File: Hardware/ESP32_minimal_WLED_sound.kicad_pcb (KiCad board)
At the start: 2 copper layers, 33.8 x 43.9 mm, 39 parts, among them J1 Conn_01x04_Male, J3 Conn_01x02_Male, Q1 AO3400A, U1 LM1117-3.3, U2 ESP32-S2-WROVER, U3 USBLC6-2SC6, U4 TXS0102DCT

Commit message: update to V1
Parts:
- removed D1: LED, LED_SMD:LED_0603_1608Metric
- removed FB1, FB2: >1A, Inductor_SMD:L_0603_1608Metric
- removed JP2: SolderJumper_3_Bridged12, Jumper:SolderJumper-3_P1.3mm_Bridged12_Pad1.0x1.5mm
- added G***: LOGO, LOGO, B.Cu at (123.6, 68.5)
- added J2: USB_C_Receptacle_USB2.0, Connector_USB:USB_C_Receptacle_HRO_TYPE-C-31-M-12, F.Cu at (145.0, 67.0)
- added J4: Barrel_Jack_Switch_Pin3Ring, Connector_BarrelJack:BarrelJack_GCT_DCJ200-10-A_Horizontal, F.Cu at (142.1, 85.2)
- added J5: Conn_01x03_Male, Connector_JST:JST_EH_B3B-EH-A_1x03_P2.50mm_Vertical, F.Cu at (119.4, 88.9)
- added J6: Conn_01x03_Male, Connector_JST:JST_EH_B3B-EH-A_1x03_P2.50mm_Vertical, F.Cu at (119.4, 93.5)
- added J7: Conn_01x03_Male, Connector_PinHeader_2.54mm:PinHeader_1x03_P2.54mm_Vertical, F.Cu at (119.4, 88.9)
- added J8: Conn_01x02_Male, TerminalBlock_Phoenix:TerminalBlock_Phoenix_MKDS-1,5-2-5.08_1x02_P5.08mm_Horizontal, F.Cu at (137.6, 91.0)
- added J9: Conn_01x03_Male, Connector_PinHeader_2.54mm:PinHeader_1x03_P2.54mm_Vertical, F.Cu at (119.4, 93.5)
- added MK1: ICS-43434, ICS-43434:MIC_ICS-43434, F.Cu at (118.7, 84.1)
- added R14: 4,7k, Resistor_SMD:R_0603_1608Metric, F.Cu at (125.2, 94.4)
- added R15: 4,7k, Resistor_SMD:R_0603_1608Metric, F.Cu at (128.3, 94.4)
- added SW2: Boot, Button_Switch_SMD:SW_SPST_B3U-1000P-B, F.Cu at (128.4, 83.8)
- added U5: ESP32-WROOM-32, RF_Module:ESP32-WROOM-32, F.Cu at (124.3, 71.6)
- C1, C2: moved to B.Cu
- C10, C11: footprint Capacitor_SMD:C_0603_1608Metric_Pad1.08x0.95mm_HandSolder -> Capacitor_SMD:C_0603_1608Metric
- C3, C4: value 20p -> 0.1uF; footprint Capacitor_SMD:C_0603_1608Metric -> Capacitor_SMD:C_0805_2012Metric; moved to B.Cu
- C5: value 0.1u -> 0.1uF
- C9: value 0.1u -> 0.1uF; footprint Capacitor_SMD:C_0603_1608Metric -> Capacitor_SMD:C_0805_2012Metric
- J1: footprint Connector_PinHeader_2.54mm:PinHeader_1x04_P2.54mm_Horizontal -> Connector_PinHeader_2.54mm:PinHeader_1x04_P2.54mm_Vertical
- J3: footprint Connector_Phoenix_MSTB:PhoenixContact_MSTBA_2,5_2-G-5,08_1x02_P5.08mm_Horizontal -> TerminalBlock_Phoenix:TerminalBlock_Phoenix_MKDS-1,5-2-5.08_1x02_P5.08mm_Horizontal
- JP1: value SolderJumper_2_Bridged -> SolderJumper_3_Open; footprint Jumper:SolderJumper-2_P1.3mm_Bridged_RoundedPad1.0x1.5mm -> Jumper:SolderJumper-3_P1.3mm_Open_Pad1.0x1.5mm; moved to B.Cu
- R1: value 10k -> 1M
- R12, R13: footprint Capacitor_SMD:C_0603_1608Metric_Pad1.08x0.95mm_HandSolder -> Resistor_SMD:R_0603_1608Metric
- R2: value 100r -> 0.01; footprint Resistor_SMD:R_0603_1608Metric -> Resistor_SMD:R_0805_2012Metric
- R3, R4: value 22r -> 10
- R6, R7, R9: footprint Resistor_SMD:R_0805_2012Metric -> Resistor_SMD:R_0603_1608Metric
- R8: value 100r -> 100
- U1: value LM1117-3.3 -> LM1117-5; moved to B.Cu
- U2: value ESP32-S2-WROVER -> INA226; footprint RF_Module:ESP32-S2-WROVER -> Package_SO:VSSOP-10_3x3mm_P0.5mm
- U3: value USBLC6-2SC6 -> LM1117-3.3; footprint Package_TO_SOT_SMD:SOT-23-6 -> Package_TO_SOT_SMD:SOT-223; moved to B.Cu
- moved R12 72.5 mm to (113.8, 83.8), turned to -90 degrees
- moved C6 68.4 mm to (131.7, 83.8), turned to -90 degrees
- moved R13 67.0 mm to (112.1, 83.8), turned to -90 degrees
- moved R4 66.9 mm to (129.6, 89.5)
- moved C7 62.1 mm to (113.8, 64.4), turned to -90 degrees
- moved R3 59.5 mm to (129.6, 91.3), turned to 180 degrees
- moved R5 58.0 mm to (112.3, 64.4), turned to -90 degrees
- moved JP1 56.6 mm to (140.1, 80.5), turned to 90 degrees
- moved C9 51.1 mm to (125.0, 85.2), turned to 90 degrees
- moved C1 50.7 mm to (137.2, 85.7), turned to 90 degrees
- moved D2 47.9 mm to (135.6, 74.8), turned to 180 degrees
- moved R2 42.8 mm to (133.6, 90.3), turned to -90 degrees
- moved J3 41.7 mm to (143.7, 80.3), turned to 90 degrees
- moved C10 39.7 mm to (113.0, 81.5)
- moved R1 39.6 mm to (141.4, 61.0), turned to 180 degrees
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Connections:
- C1 pad 1: +5V -> +12VA
- C2 pad 2: +3V3 -> +5V
- C3 pad 1: GND -> +5V
- C3 pad 2: /USB_D+ -> GND
- C4 pad 1: /USB_D- -> GND
- C4 pad 2: GND -> +3V3
- C5 pad 1: /EN -> +12VA
- C5 pad 2: GND -> +12V
- C6 pad 1: /IO00 -> IO00
- C7 pad 2: GND -> EN
- C8 pad 2: Net-(C8-Pad2) -> /U_GND
- C9 pad 1: VBUS -> +3V3
- J1 pad 2: +5VD -> Net-(J1-Pad2)
- J1 pad 3: +3V3 -> Net-(J1-Pad3)
- J1 pad 4: +12V -> +3V3
- JP1 pad 1: +3V3 -> +5V
- JP1 pad 2: Net-(JP1-Pad2) -> /O1V
- R1 pad 1: +3V3 -> /U_GND
- R1 pad 2: unconnected-(R1-Pad2) -> GND
- R12 pad 2: WS2812B_GPIO_0 -> WS2812B_2
- R13 pad 2: WS2812B_GPIO_0 -> WS2812B_4
- R2 pad 1: Net-(D1-Pad2) -> +12VA
- R2 pad 2: unconnected-(R2-Pad2) -> +12V
- R3 pad 1: /USB_D+ -> +12V
- R3 pad 2: unconnected-(R3-Pad2) -> Net-(R3-Pad2)
- R4 pad 1: /USB_D- -> Net-(R4-Pad1)
- R4 pad 2: unconnected-(R4-Pad2) -> +12VA
- R5 pad 2: /EN -> EN
- R8 pad 1: Net-(JP1-Pad2) -> +3V3
- U1 pad 2: +3V3 -> +5V
- U1 pad 3: +5V -> +12VA
- U2 pad 10: unconnected-(U2-Pad10) -> Net-(R3-Pad2)
- U2 pad 2: unconnected-(U2-Pad2) -> GND
- U2 pad 3: /IO00 -> unconnected-(U2-Pad3)
- U2 pad 4: unconnected-(U2-Pad4) -> SD
- U2 pad 5: unconnected-(U2-Pad5) -> SCK
- U2 pad 6: unconnected-(U2-Pad6) -> +3V3
- U2 pad 7: unconnected-(U2-Pad7) -> GND
- U2 pad 9: unconnected-(U2-Pad9) -> Net-(R4-Pad1)
- U3 pad 1: /D- -> GND
- U3 pad 2: GND -> +3V3
- U3 pad 3: /D+ -> +5V
- U3 pad 4: /USB_D+ -> (no net)
- U4 pad 4: GPIO_0 -> GPIO_4
- U4 pad 5: GPIO_0 -> GPIO_2
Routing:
- net +3V3: track 0.00 -> 96.4 mm, vias 0 -> 2
- net +5V: track 0.00 -> 95.5 mm, vias 0 -> 3
- net SD: track 0.00 -> 48.6 mm, vias 0 -> 3
- net +12VA: track 0.00 -> 37.9 mm, vias 0 -> 3
- net SCK: track 0.00 -> 23.7 mm, vias 0 -> 2
- net GPIO_4: track 0.00 -> 21.5 mm, vias 0 -> 2
- net GPIO_2: track 0.00 -> 19.9 mm, vias 0 -> 2
- net +12V: track 0.00 -> 15.4 mm
- net GND: track 0.00 -> 15.0 mm, vias 0 -> 21
- net WS: track 0.00 -> 14.7 mm
- net /O1: track 0.00 -> 13.0 mm
- net /O1V: track 0.00 -> 11.2 mm
- net WS2812B_4: track 0.00 -> 10.8 mm
- net Net-(R12-Pad1): track 0.00 -> 7.82 mm, vias 0 -> 2
- net Net-(Q1-Pad2): track 0.00 -> 7.21 mm
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- added copper zone on F.Cu, net /U_GND
- added copper zone on B.Cu, net GND
- added copper zone on F.Cu, net GND
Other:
- board size 33.8 x 43.9 mm -> 37.4 x 39.8 mm
- board text added: "ESP32_minimal_WLED_sound V1"

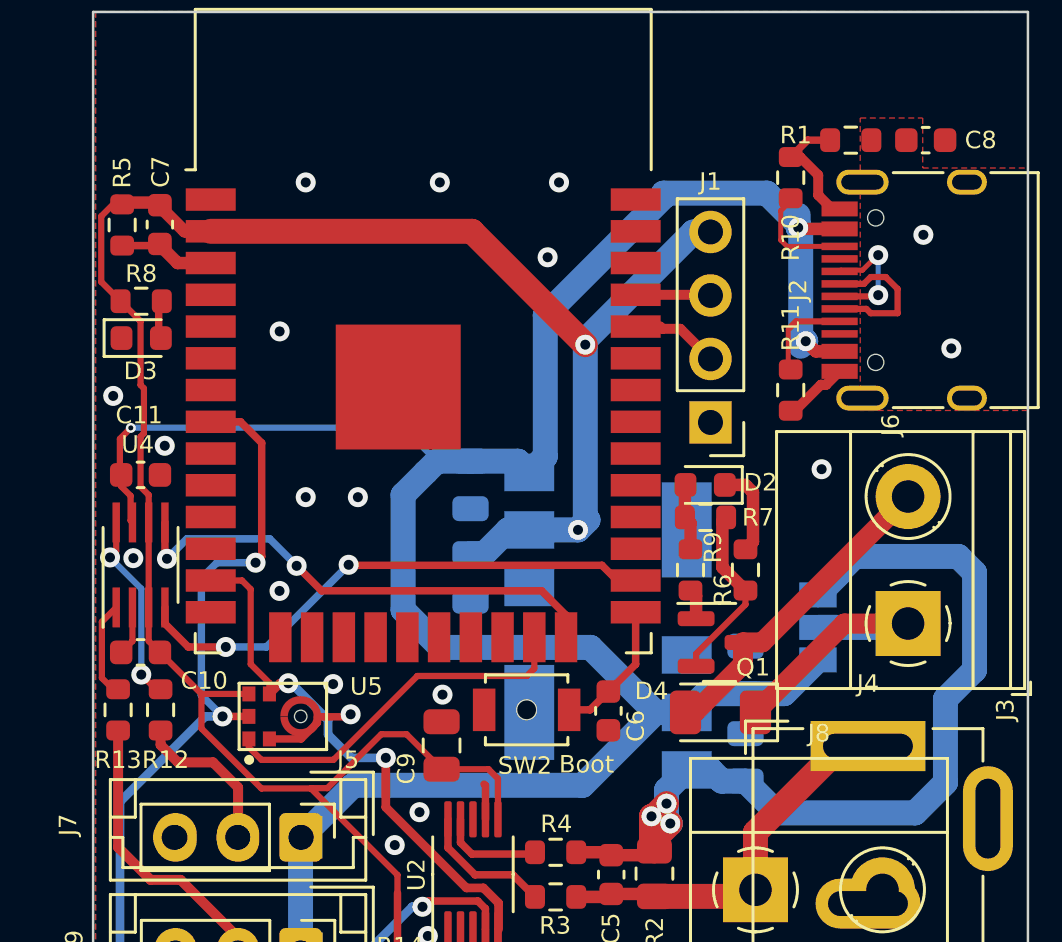
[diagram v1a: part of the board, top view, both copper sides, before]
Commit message: fix esp32 EN and IO0, Todo: solder jumper and 12V to 5V
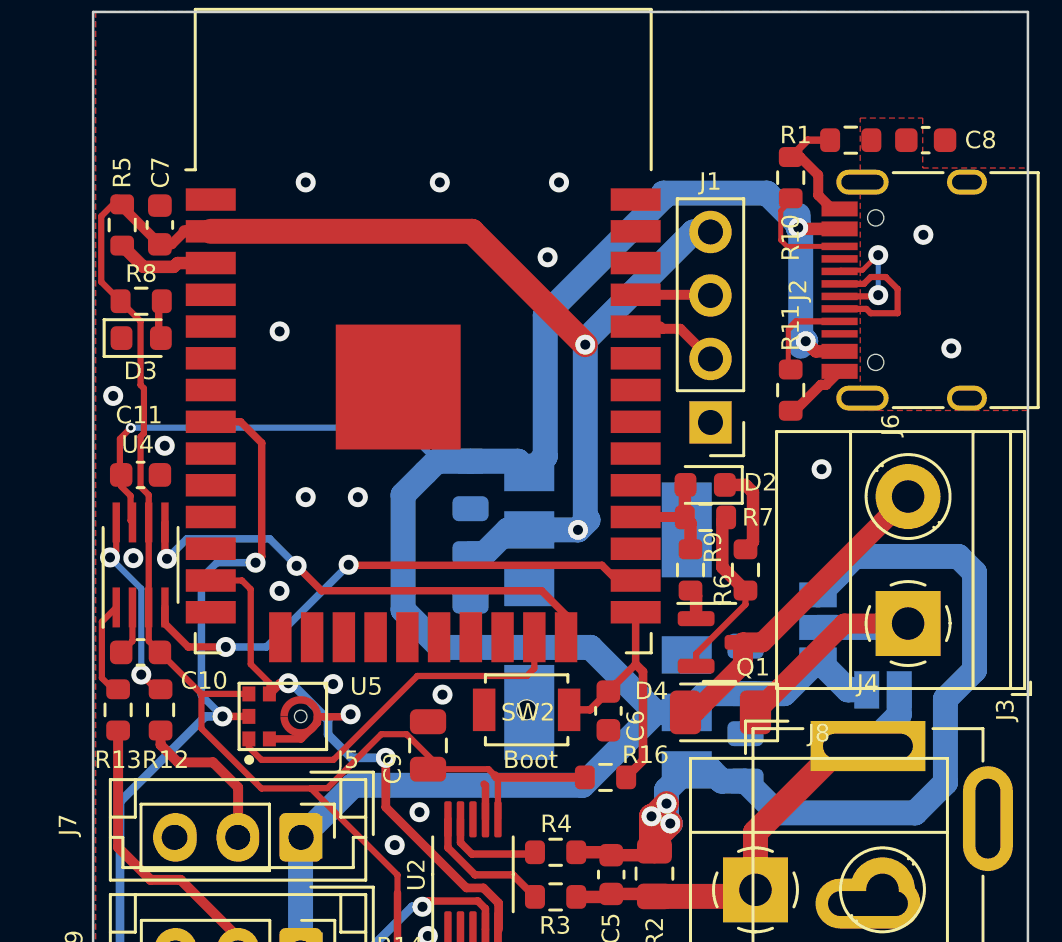
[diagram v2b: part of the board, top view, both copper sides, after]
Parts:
- added JP2: SolderJumper_2_Open, Jumper:SolderJumper-2_P1.3mm_Open_Pad1.0x1.5mm, B.Cu at (142.7, 83.0)
- added R16: 10k, Resistor_SMD:R_0603_1608Metric, F.Cu at (131.6, 86.5)
- moved C9 0.54 mm to (124.5, 85.2)
- turned C7 to 90 degrees
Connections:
- C7 pad 2: EN -> GND
- D2 pad 2: /M1 -> M1
- R7 pad 1: /M1 -> M1
- R9 pad 1: /M1 -> M1
- U5 pad 28: unconnected-(U5-Pad28) -> M1
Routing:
- net IO00: track 5.50 -> 10.4 mm
- net M1: track 0.00 -> 4.65 mm
- net +3V3: track 96.4 -> 100.3 mm
- net +12V: track 15.4 -> 18.2 mm
- net /M1: track 2.68 -> 0.00 mm
- net +5V: track 95.5 -> 97.9 mm

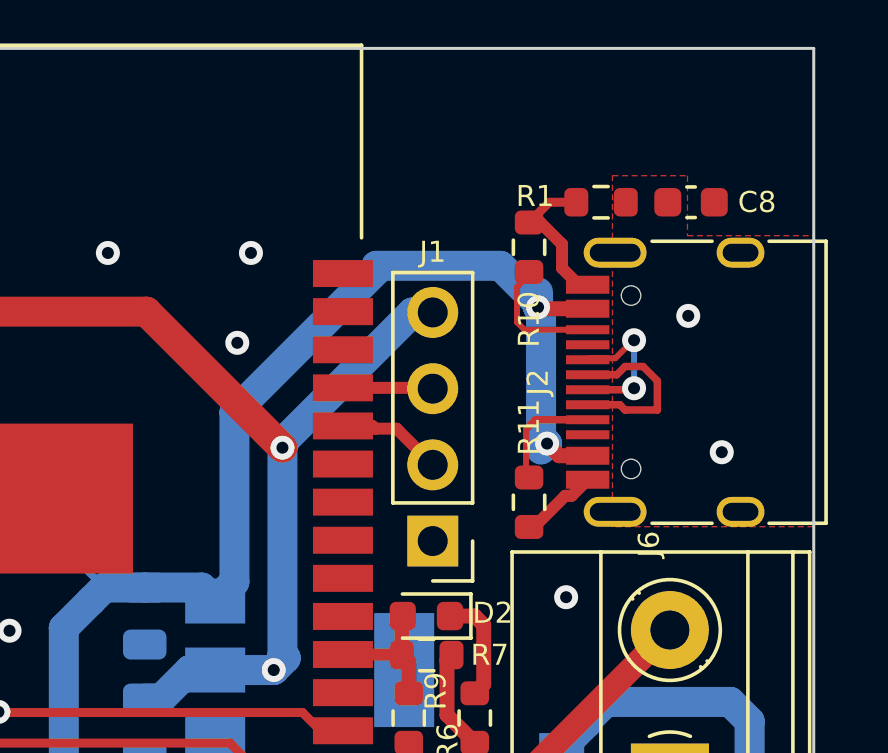
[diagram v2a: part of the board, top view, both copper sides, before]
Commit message: update esphome config
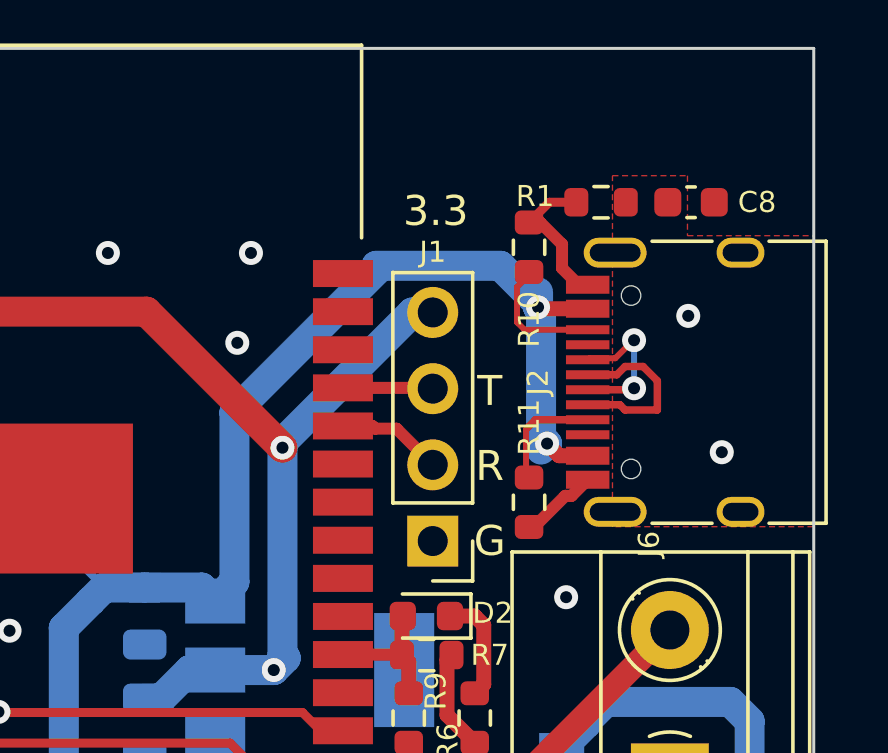
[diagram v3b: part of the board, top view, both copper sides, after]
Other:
- board text added: "3.3"
- board text added: "5V"
- board text added: "D2"
- board text added: "D4"
- board text added: "ESP32_minimal_WLED_sound V2"
- board text added: "G"
- board text added: "GND"
- board text added: "R"
- board text added: "T"
- board text removed: "ESP32_minimal_WLED_sound V1"
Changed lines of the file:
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@@
   )
   (gr_rect (start 111.1 55.878023) (end 148.5 95.7) (layer "Edge.Cuts") (width 0.1) (fill none))
-  (gr_text "ESP32_minimal_WLED_sound\nV1" (at 128.594063 58.872073) (layer "B.SilkS")
+  (gr_text "GND" (at 114.1 91.3) (layer "B.SilkS")
+    (effects (font (size 1 1) (thickness 0.15)) (justify mirror))
+  )
+  (gr_text "ESP32_minimal_WLED_sound\nV2" (at 128.594063 58.872073) (layer "B.SilkS")
     (effects (font (size 1.5 1.5) (thickness 0.3)) (justify mirror))
   )
+  (gr_text "D2" (at 116.9 86.4) (layer "B.SilkS")
+    (effects (font (size 1 1) (thickness 0.15)) (justify mirror))
+  )
+  (gr_text "D4" (at 116.8 91.3) (layer "B.SilkS")
+    (effects (font (size 1 1) (thickness 0.15)) (justify mirror))
+  )
+  (gr_text "5V" (at 119.3 91.3) (layer "B.SilkS")
+    (effects (font (size 1 1) (thickness 0.15)) (justify mirror))
+  )
+  (gr_text "R" (at 137.7 69.8) (layer "F.SilkS")
+    (effects (font (size 1 1) (thickness 0.15)))
+  )
+  (gr_text "T" (at 137.7 67.3) (layer "F.SilkS")
+    (effects (font (size 1 1) (thickness 0.15)))
+  )
+  (gr_text "G" (at 137.7 72.3) (layer "F.SilkS")
+    (effects (font (size 1 1) (thickness 0.15)))
+  )
+  (gr_text "3.3" (at 135.9 61.3) (layer "F.SilkS")
+    (effects (font (size 1 1) (thickness 0.15)))
+  )
   (segment (start 139.360185 64.556724) (end 139.310185 64.506724) (width 0.5) (layer "F.Cu") (net 1))

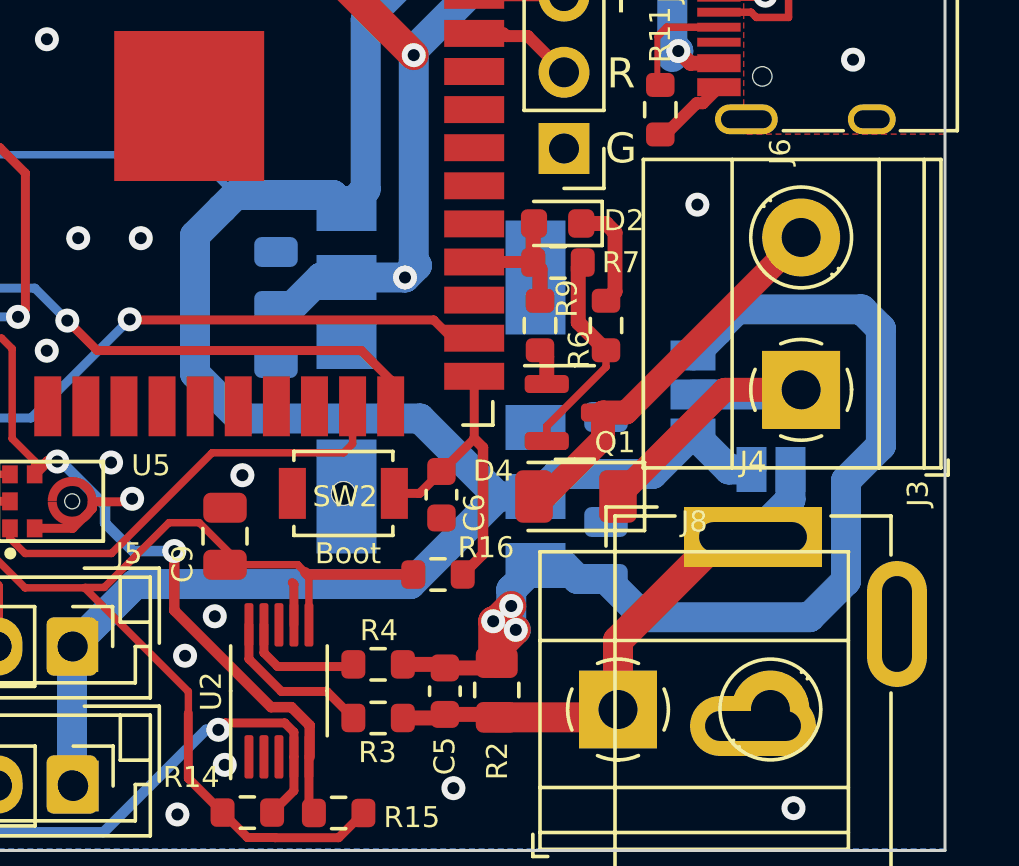
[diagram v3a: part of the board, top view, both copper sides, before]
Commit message: switch 12V to 5V to DCDC
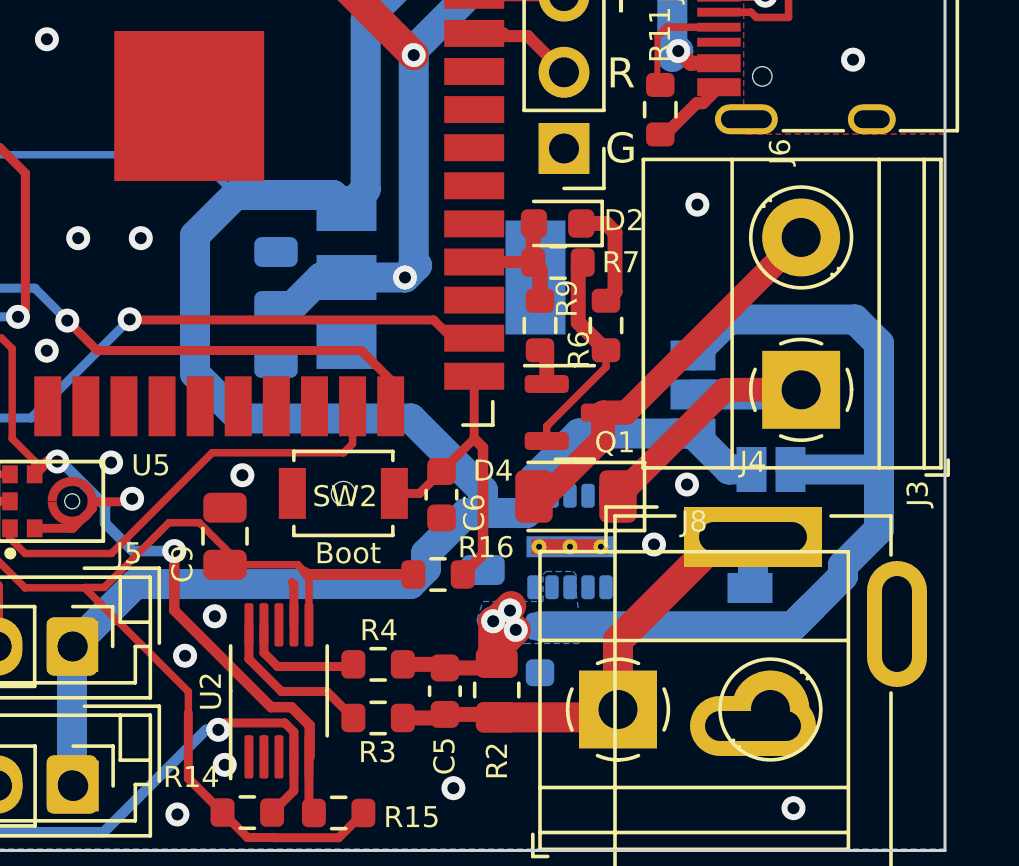
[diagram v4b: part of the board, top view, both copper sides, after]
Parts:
- added JP3: SolderJumper_2_Open, Jumper:SolderJumper-2_P1.3mm_Open_Pad1.0x1.5mm, B.Cu at (142.0, 87.6)
- C1: value 0.1uF -> 10uF; footprint Capacitor_SMD:C_0805_2012Metric -> Capacitor_SMD:C_0603_1608Metric
- C2: value 0.1uF -> 22uF
- U1: value LM1117-5 -> LMZM23601V5; footprint Package_TO_SOT_SMD:SOT-223 -> Package_LGA:Texas_SIL0010A_MicroSiP-10-1EP_3.8x3mm_P0.6mm_EP0.7x2.9mm_ThermalVias
- moved C2 5.20 mm to (133.1, 85.4)
- moved U1 4.55 mm to (136.0, 85.4), turned to 90 degrees
- moved C1 3.97 mm to (135.0, 89.0), turned to -90 degrees
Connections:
- C2 pad 1: GND -> +5V
- C2 pad 2: +5V -> GND
- JP2 pad 1: +12V -> +12VA
- Q1 pad 2: Net-(Q1-Pad2) -> GND
- R6 pad 2: Net-(Q1-Pad2) -> GND
- R7 pad 2: Net-(Q1-Pad2) -> GND
- U1 pad 2: +5V -> GND
- U1 pad 4: (no net) -> +12VA
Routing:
- net Net-(Q1-Pad2): track 7.21 -> 0.00 mm
- net GND: track 15.0 -> 22.2 mm, vias 21 -> 23
- net +12VA: track 37.9 -> 36.5 mm
- net +5V: track 97.9 -> 99.0 mm
- net +12V: track 18.2 -> 17.2 mm
- added copper zone on B.Cu, net +12VA
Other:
- board text added: "12V"
- board text added: "12VA"
